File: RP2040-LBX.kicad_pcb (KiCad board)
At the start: 2 copper layers, 288.8 x 160.1 mm, 64 parts, among them J1 USB C Connector, J2 JTAG_TC2030, SW1 Boot, U1 XC6206, U2 USBLC6-2SC6, U3 RP2040, U4 W25Q128JVS, Y1 12MHz

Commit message: move switch connects to correct relative placement
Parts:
- moved CH1 361.5 mm to (27.3, -214.8)
- moved CH2 359.0 mm to (-155.1, -183.9), turned to -9 degrees
- moved CH3 357.5 mm to (-119.6, -199.6), turned to -9 degrees
- moved CH4 352.3 mm to (-83.0, -196.9), turned to -9 degrees
- moved CH5 344.9 mm to (-51.2, -177.0), turned to -9 degrees
- moved CH7 326.4 mm to (133.4, -233.1), turned to 9 degrees
- moved CH6 325.9 mm to (101.4, -212.6), turned to 9 degrees
- moved CH8 323.1 mm to (169.9, -235.1), turned to 9 degrees
- moved CH17 322.0 mm to (81.2, -139.5), turned to 9 degrees
- moved CH16 321.2 mm to (54.8, -114.9), turned to 9 degrees
- moved CH14 319.8 mm to (-30.2, -100.2), turned to -9 degrees
- moved CH11 319.0 mm to (138.8, -198.0), turned to 9 degrees
- moved CH10 318.5 mm to (106.9, -177.2), turned to 9 degrees
- moved CH9 316.2 mm to (206.8, -219.9), turned to 9 degrees
- moved CH12 315.1 mm to (175.5, -199.6), turned to 9 degrees
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
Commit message: rescale switch connectors to proper proportion
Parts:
- moved J1 293.8 mm to (199.9, 23.0)
- moved CH2 118.0 mm to (-37.2, -178.6)
- moved CH3 108.9 mm to (-11.1, -190.1)
- moved CH4 99.2 mm to (15.7, -188.1)
- moved CH5 90.4 mm to (39.1, -173.5)
- moved CH14 86.4 mm to (54.6, -117.1)
- moved CH15 81.4 mm to (73.4, -99.0)
- moved CH21 77.3 mm to (78.1, -128.6)
- moved CH1 70.8 mm to (96.8, -201.3)
- moved CH18 65.0 mm to (121.5, -98.7)
- moved CH16 63.5 mm to (117.0, -127.9)
- moved CH19 56.5 mm to (140.2, -116.6)
- moved CH17 55.6 mm to (136.4, -146.0)
- moved CH6 51.5 mm to (151.2, -199.7)
- moved CH10 48.5 mm to (155.3, -173.7)
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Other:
- board size 288.8 x 160.1 mm -> 890.8 x 459.1 mm

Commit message: update from schematic and put edge cuts in place
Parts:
- removed H1: qw-logo, qw-logo:qw new logo silk + copper md
- removed H2: 1999 logo, 1999:1999 logo md
- removed REF**: GRAM_LOGO, MicroGRAM:GRAM_LOGO
- added SW_BOOTSEL1: SW_Push, ul_TS-1187A-B-A-B:TS-1187A-B-A-B_XKB, F.Cu at (379.5, -162.1)
- added SW_HOME1: SW_Push, ul_TS-1187A-B-A-B:TS-1187A-B-A-B_XKB, F.Cu at (379.5, -153.8)
- added SW_L3: SW_Push, ul_TS-1187A-B-A-B:TS-1187A-B-A-B_XKB, F.Cu at (379.5, -145.4)
- added SW_PSTOUCH1: SW_Push, ul_TS-1187A-B-A-B:TS-1187A-B-A-B_XKB, F.Cu at (379.5, -137.1)
- added SW_R3: SW_Push, ul_TS-1187A-B-A-B:TS-1187A-B-A-B_XKB, F.Cu at (379.5, -128.8)
- CH1, CH10, CH11, CH12, CH13, CH14, CH15, CH16, CH17, CH18, CH19, CH2, CH20, CH21, CH3, CH4, CH5, CH6, CH7, CH8, CH9: footprint MicroGRAM:Kailh_socket_PG1350 -> PCM_marbastlib-choc:SW_choc_v1_HS_1u; moved to B.Cu
- moved J1 369.5 mm to (569.4, 25.3)
- moved C12 368.1 mm to (565.6, 53.7)
- moved C16 368.1 mm to (562.9, 55.0)
- moved C17 368.1 mm to (562.9, 56.5)
- moved C3 368.1 mm to (572.9, 46.7)
- moved C7 368.1 mm to (575.1, 71.4)
- moved J2 368.1 mm to (562.1, 71.2)
- moved R10 368.1 mm to (582.1, 44.8)
- moved R11 368.1 mm to (570.5, 67.6)
- moved R3 368.1 mm to (567.4, 33.1)
- moved R7 368.1 mm to (563.5, 67.0)
- moved R8 368.1 mm to (568.9, 48.2)
- moved C10 368.1 mm to (569.4, 52.0)
- moved C14 368.1 mm to (568.5, 67.6)
- moved C15 368.1 mm to (575.5, 62.2)
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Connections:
- R10 pad 1: /~{USB_BOOT} -> USB_BOOT
- R10 pad 2: CS -> Net-(U4-~{CS})
- U3 pad 56: CS -> USB_BOOT
- U4 pad 1: CS -> Net-(U4-~{CS})
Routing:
- net CS: track 20.7 -> 0.00 mm
- net (no net): track 0.00 -> 20.7 mm
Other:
- board size 890.8 x 459.1 mm -> 292.7 x 140.6 mm
- board text removed: "100nF"
- board text removed: "GRAM-SLIM v3.2 PCB by Quark x GRAM 19.99"
- board text removed: "RP2040"
- board text removed: "x"

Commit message: move the placement of hotswap sockets slightly into position (eyeballed)
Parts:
- moved CH1 1.80 mm to (200.2, 84.0)
- moved CH10 1.80 mm to (258.6, 111.6)
- moved CH11 1.80 mm to (282.1, 96.3)
- moved CH12 1.80 mm to (309.0, 95.2)
- moved CH13 1.80 mm to (336.1, 106.2)
- moved CH14 1.80 mm to (157.9, 168.2)
- moved CH15 1.80 mm to (176.7, 186.2)
- moved CH16 1.80 mm to (220.4, 157.3)
- moved CH17 1.80 mm to (239.8, 139.3)
- moved CH18 1.80 mm to (224.9, 186.6)
- moved CH19 1.80 mm to (243.6, 168.7)
- moved CH2 1.80 mm to (66.2, 106.7)
- moved CH20 1.80 mm to (263.1, 150.5)
- moved CH21 1.80 mm to (181.4, 156.6)
- moved CH3 1.80 mm to (92.2, 95.1)
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
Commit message: place mcu components and route buttons
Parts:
- removed SW1: Boot, Button_Switch_SMD:SW_SPST_SKQG_WithStem
- C1, C10, C11, C12, C13, C14, C15, C16, C17, C2, C3, C4, C5, C6, C7, C8, C9, D1, D2, D3, F1, J1, J2, R1, R10, R11, R2, R3, R4, R5, R6, R7, R8, R9, U1, U2, U3, U4, Y1: moved to F.Cu
- moved R10 397.2 mm to (190.0, 108.1)
- moved U4 390.1 mm to (193.6, 111.9), turned to 0 degrees
- moved C15 384.1 mm to (196.6, 125.5), turned to -135 degrees
- moved C7 383.3 mm to (197.0, 134.7)
- moved C13 382.4 mm to (197.5, 119.6)
- moved C3 378.9 mm to (199.2, 110.0), turned to 0 degrees
- moved Y1 376.6 mm to (200.4, 134.4), turned to 180 degrees
- moved R2 375.4 mm to (197.4, 66.3), turned to 180 degrees
- moved C5 375.1 mm to (201.2, 115.2)
- moved R11 374.3 mm to (201.6, 130.9)
- moved C10 372.1 mm to (202.7, 115.2)
- moved U2 372.1 mm to (202.7, 105.7)
- moved U3 372.1 mm to (202.7, 123.3), turned to 0 degrees
- moved J1 371.5 mm to (199.4, 58.5), turned to 180 degrees
- moved R8 371.2 mm to (203.1, 111.5)
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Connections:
- U3 pad 56: USB_BOOT -> Net-(U4-~{CS})
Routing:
- net C_LT: track 248.1 -> 53.3 mm, vias 2 -> 1
- net C_DN: track 266.3 -> 88.5 mm, vias 2 -> 1
- net A: track 229.1 -> 93.2 mm, vias 2 -> 1
- net C_UP: track 196.9 -> 67.9 mm, vias 2 -> 1
- net C_RT: track 205.8 -> 78.3 mm, vias 2 -> 1
- net M2: track 186.9 -> 67.1 mm, vias 2 -> 1
- net EXTRA: track 137.8 -> 39.3 mm, vias 2 -> 1
- net M1: track 168.6 -> 72.5 mm, vias 2 -> 1
- net RIGHT: track 129.4 -> 53.3 mm, vias 0 -> 1
- net 3vCable: track 46.6 -> 111.5 mm
- net L: track 185.4 -> 131.9 mm, vias 0 -> 1
- net Y: track 152.4 -> 105.3 mm, vias 2 -> 1
- net B: track 112.2 -> 68.6 mm, vias 2 -> 1
- net LS: track 179.5 -> 136.7 mm, vias 2 -> 1
- net MS: track 203.2 -> 163.4 mm, vias 2 -> 1
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- added copper zone on F.Cu, net +1V1
- added copper zone on F.Cu, net +3V3
- removed copper zone on B.Cu, net +1V1
- removed copper zone on B.Cu, net +3V3

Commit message: place and route extra switches
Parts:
- moved SW_R3 343.8 mm to (94.1, 62.9)
- moved SW_PSTOUCH1 340.8 mm to (103.6, 62.9)
- moved SW_L3 338.3 mm to (113.0, 62.9)
- moved SW_HOME1 336.2 mm to (122.4, 62.9)
- moved SW_BOOTSEL1 334.6 mm to (131.9, 62.9)
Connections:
- net Net-(U4-~{CS}) renamed CS
- SW_BOOTSEL1 pad 2: GND -> USB_BOOT
- SW_BOOTSEL1 pad 3: (no net) -> GND
- SW_BOOTSEL1 pad 4: (no net) -> GND
- SW_HOME1 pad 2: GND -> SW_HOME
- SW_HOME1 pad 3: (no net) -> GND
- SW_HOME1 pad 4: (no net) -> GND
- SW_L3 pad 2: GND -> SW_L3
- SW_L3 pad 3: (no net) -> GND
- SW_L3 pad 4: (no net) -> GND
- SW_PSTOUCH1 pad 2: GND -> SW_PSTOUCH
- SW_PSTOUCH1 pad 3: (no net) -> GND
- SW_PSTOUCH1 pad 4: (no net) -> GND
- SW_R3 pad 2: GND -> SW_R3
- SW_R3 pad 3: (no net) -> GND
- SW_R3 pad 4: (no net) -> GND
- U3 pad 11: unconnected-(U3-GPIO8-Pad11) -> SW_HOME
- U3 pad 12: unconnected-(U3-GPIO9-Pad12) -> SW_L3
- U3 pad 13: unconnected-(U3-GPIO10-Pad13) -> SW_PSTOUCH
- U3 pad 14: unconnected-(U3-GPIO11-Pad14) -> SW_R3
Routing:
- net SW_R3: track 0.00 -> 137.2 mm
- net SW_PSTOUCH: track 0.00 -> 127.6 mm
- net SW_L3: track 0.00 -> 112.0 mm
- net SW_HOME: track 0.00 -> 108.4 mm
- net USB_BOOT: track 0.01 -> 80.4 mm
- net 3vCable: track 111.5 -> 107.5 mm
- net +3V3: track 67.8 -> 67.2 mm

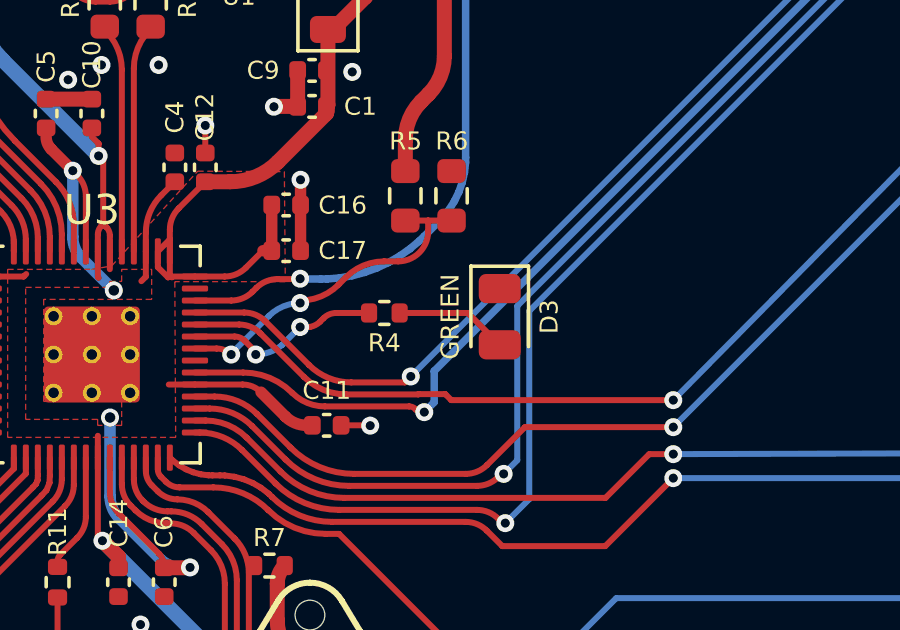
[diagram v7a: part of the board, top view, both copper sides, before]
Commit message: push the led closer to the middle
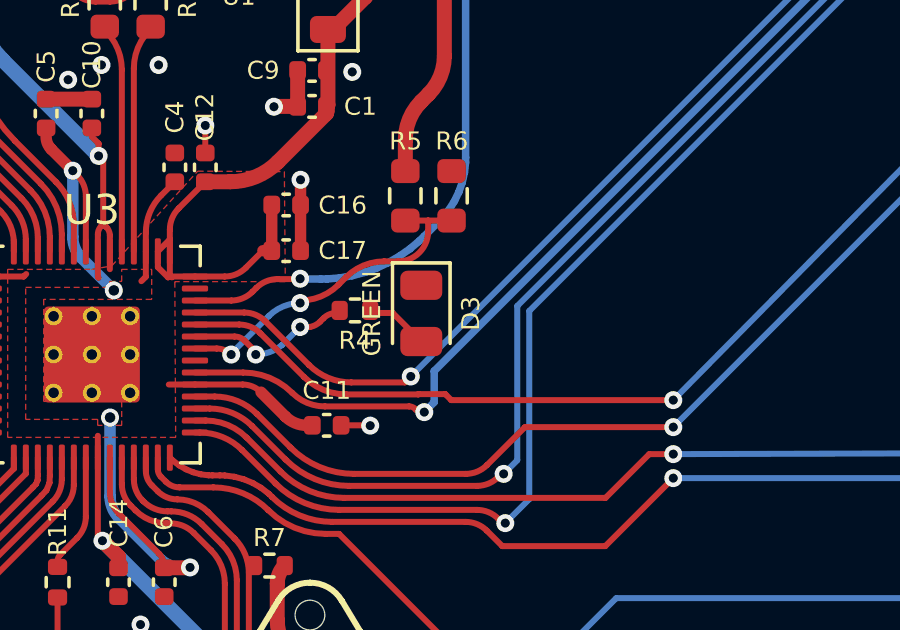
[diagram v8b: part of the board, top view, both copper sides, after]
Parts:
- moved D3 2.62 mm to (213.7, 121.9)
- moved R4 0.98 mm to (211.5, 121.8)
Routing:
- net Net-(D3-A): track 3.78 -> 2.13 mm
- net PICO_LED: track 6.53 -> 5.58 mm
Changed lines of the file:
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@@
 	(footprint "Resistor_SMD:R_0402_1005Metric"
 		(layer "F.Cu")
-		(at 212.46825 121.895)
+		(at 211.49 121.81)
 		(descr "Resistor SMD 0402 (1005 Metric), square (rectangular) end terminal, IPC_7351 nominal, (Body size source: IPC-SM-782 page 72, https://www.pcb-3d.com/wordpress/wp-content/uploads/ipc-sm-782a_amendment_1_and_2.pdf), generated with kicad-footprint-generator")
 		(tags "resistor")
@@
 	(footprint "LED_SMD:LED_0805_2012Metric"
 		(layer "F.Cu")
-		(at 216.314657 122.01995 -90)
+		(at 213.7 121.91 -90)
 		(descr "LED SMD 0805 (2012 Metric), square (rectangular) end terminal, IPC_7351 nominal, (Body size source: https://docs.google.com/spreadsheets/d/1BsfQQcO9C6DZCsRaXUlFlo91Tg2WpOkGARC1WS5S8t0/edit?usp=sharing), generated with kicad-footprint-generator")
 		(tags "LED")
@@
 	)
 	(segment
-		(start 210.8646 121.895)
-		(end 211.95825 121.895)
+		(start 210.895 121.895)
+		(end 210.98 121.81)
 		(width 0.2)
 		(layer "F.Cu")
@@
 	)
 	(segment
-		(start 210.323538 122.187534)
-		(end 210.440336 122.070736)
+		(start 208.182161 123.188911)
+		(end 207.812999 122.819718)
 		(width 0.2)
 		(layer "F.Cu")
@@
 	)
 	(segment
-		(start 208.182161 123.188911)
-		(end 207.812999 122.819718)
+		(start 210.323538 122.187534)
+		(end 210.440336 122.070736)
 		(width 0.2)
 		(layer "F.Cu")
@@
 	)
 	(segment
-		(start 209.663242 122.361397)
-		(end 209.978018 122.361397)
+		(start 210.8646 121.895)
+		(end 210.895 121.895)
 		(width 0.2)
 		(layer "F.Cu")
@@
 		(net "PICO_LED")
 	)
+	(segment
+		(start 209.663242 122.361397)
+		(end 209.978018 122.361397)
+		(width 0.2)
+		(layer "F.Cu")
+		(net "PICO_LED")
+	)
 	(via
 		(at 209.661364 122.363275)
@@
 	)
 	(arc
-		(start 209.978018 122.361397)
-		(mid 210.16465 122.301405)
-		(end 210.323538 122.187534)
+		(start 210.440336 122.070736)
+		(mid 210.63499 121.940672)
+		(end 210.8646 121.895)
 		(width 0.2)
 		(layer "F.Cu")
@@
 	)
 	(arc
-		(start 210.440336 122.070736)
-		(mid 210.63499 121.940672)
-		(end 210.8646 121.895)
+		(start 209.978018 122.361397)
+		(mid 210.16465 122.301405)
+		(end 210.323538 122.187534)
 		(width 0.2)
 		(layer "F.Cu")
@@
 	)
 	(segment
-		(start 215.252207 121.895)
-		(end 216.314657 122.95745)
+		(start 212 121.81)
+		(end 212.085 121.895)
+		(width 0.2)
+		(layer "F.Cu")
+		(net "Net-(D3-A)")
+	)
+	(segment
+		(start 212.7475 121.895)
+		(end 213.7 122.8475)
 		(width 0.2)
 		(layer "F.Cu")
@@
 	)
 	(segment
-		(start 212.97825 121.895)
-		(end 215.252207 121.895)
+		(start 212.085 121.895)
+		(end 212.7475 121.895)
 		(width 0.2)
 		(layer "F.Cu")
@@
 	)
 	(segment
-		(start 107.848848 64.114)
-		(end 172.234848 128.5)
+		(start 107.732448 61.045)
+		(end 106.571077 61.045)
 		(width 0.2)
 		(layer "F.Cu")
-		(net "SW_R3")
+		(net "SW_PSTOUCH")
 	)
 	(segment
-		(start 172.234848 128.5)
-		(end 196.66075 128.5)
+		(start 199.28075 125.48)
+		(end 198.74689 125.48)
 		(width 0.2)
 		(layer "F.Cu")
-		(net "SW_R3")
+		(net "SW_PSTOUCH")
 	)
 	(segment
-		(start 97.136002 61.045)
-		(end 91.135998 61.045)
+		(start 196.12689 128.1)
+		(end 174.787448 128.1)
 		(width 0.2)
 		(layer "F.Cu")
-		(net "SW_R3")
+		(net "SW_PSTOUCH")
 	)
 	(segment
-		(start 97.136002 61.045)
-		(end 100.205002 64.114)
+		(start 106.571077 61.045)
+		(end 100.571073 61.045)
 		(width 0.2)
 		(layer "F.Cu")
-		(net "SW_R3")
+		(net "SW_PSTOUCH")
 	)
 	(segment
-		(start 100.205002 64.114)
-		(end 107.848848 64.114)
+		(start 198.74689 125.48)
+		(end 196.12689 128.1)
 		(width 0.2)
 		(layer "F.Cu")
-		(net "SW_R3")
+		(net "SW_PSTOUCH")
 	)
 	(segment
-		(start 196.66075 128.5)
-		(end 199.28075 125.88)
+		(start 174.787448 128.1)
+		(end 107.732448 61.045)
 		(width 0.2)
 		(layer "F.Cu")
-		(net "SW_R3")
+		(net "SW_PSTOUCH")
 	)
 	(segment
-		(start 107.732448 61.045)
-		(end 106.571077 61.045)
+		(start 107.848848 64.114)
+		(end 172.234848 128.5)
 		(width 0.2)
 		(layer "F.Cu")
-		(net "SW_PSTOUCH")
+		(net "SW_R3")
 	)
 	(segment
-		(start 199.28075 125.48)
-		(end 198.74689 125.48)
+		(start 172.234848 128.5)
+		(end 196.66075 128.5)
 		(width 0.2)
 		(layer "F.Cu")
-		(net "SW_PSTOUCH")
+		(net "SW_R3")
 	)
 	(segment
-		(start 196.12689 128.1)
-		(end 174.787448 128.1)
+		(start 97.136002 61.045)
+		(end 91.135998 61.045)
 		(width 0.2)
 		(layer "F.Cu")
-		(net "SW_PSTOUCH")
+		(net "SW_R3")
 	)
 	(segment
-		(start 106.571077 61.045)
-		(end 100.571073 61.045)
+		(start 97.136002 61.045)
+		(end 100.205002 64.114)
 		(width 0.2)
 		(layer "F.Cu")
-		(net "SW_PSTOUCH")
+		(net "SW_R3")
 	)
 	(segment
-		(start 198.74689 125.48)
-		(end 196.12689 128.1)
+		(start 100.205002 64.114)
+		(end 107.848848 64.114)
 		(width 0.2)
 		(layer "F.Cu")
-		(net "SW_PSTOUCH")
+		(net "SW_R3")
 	)
 	(segment
-		(start 174.787448 128.1)
-		(end 107.732448 61.045)
+		(start 196.66075 128.5)
+		(end 199.28075 125.88)
 		(width 0.2)
 		(layer "F.Cu")
-		(net "SW_PSTOUCH")
+		(net "SW_R3")
 	)
 	(segment
